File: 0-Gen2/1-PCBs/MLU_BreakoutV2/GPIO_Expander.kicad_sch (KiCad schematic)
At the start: 8 parts, among them U7 MCP23008-E_P

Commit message: [final pass] MLU breakout
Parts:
- JP10, JP8, JP9: footprint Jumper:SolderJumper-3_P1.3mm_Bridged2Bar12_RoundedPad1.0x1.5mm -> Connector_PinHeader_1.27mm:PinHeader_1x03_P1.27mm_Vertical
- U7: footprint Imported Footprints:MCP3008 -> ImportedV2:MCP3008
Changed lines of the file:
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@@
 			)
 		)
-		(property "Footprint" "Jumper:SolderJumper-3_P1.3mm_Bridged2Bar12_RoundedPad1.0x1.5mm"
+		(property "Footprint" "Connector_PinHeader_1.27mm:PinHeader_1x03_P1.27mm_Vertical"
 			(at 93.98 75.946 0)
 			(effects
@@
 			)
 		)
-		(property "Footprint" "Imported Footprints:MCP3008"
+		(property "Footprint" "ImportedV2:MCP3008"
 			(at 163.322 92.71 0)
 			(effects
@@
 			)
 		)
-		(property "Footprint" "Jumper:SolderJumper-3_P1.3mm_Bridged2Bar12_RoundedPad1.0x1.5mm"
+		(property "Footprint" "Connector_PinHeader_1.27mm:PinHeader_1x03_P1.27mm_Vertical"
 			(at 75.438 83.82 0)
 			(effects
@@
 			)
 		)
-		(property "Footprint" "Jumper:SolderJumper-3_P1.3mm_Bridged2Bar12_RoundedPad1.0x1.5mm"
+		(property "Footprint" "Connector_PinHeader_1.27mm:PinHeader_1x03_P1.27mm_Vertical"
 			(at 111.76 111.252 0)
 			(effects

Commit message: before restructure
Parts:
- renumbered C3 to C1, C4 to C2, C5 to C3, JP8 to JP11, JP9 to JP12, JP10 to JP13, U7 to U2
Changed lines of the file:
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@@
 		(dnp no)
 		(fields_autoplaced yes)
-		(property "Reference" "JP8"
+		(property "Reference" "JP11"
 			(at 93.98 72.644 0)
 			(effects
@@
 			(project "MLU_BreakoutV2"
 				(path "/55121ba7-5d22-4fe3-93aa-7f76d75b410c/ff819628-ab19-4c4a-a87c-3aa1c78e0ae1"
-					(reference "JP8")
+					(reference "JP11")
 					(unit 1)
 				)
@@
 		(on_board yes)
 		(dnp no)
-		(property "Reference" "C4"
+		(property "Reference" "C2"
 			(at 120.142 115.8239 0)
 			(effects
@@
 			(project "MLU_BreakoutV2"
 				(path "/55121ba7-5d22-4fe3-93aa-7f76d75b410c/ff819628-ab19-4c4a-a87c-3aa1c78e0ae1"
-					(reference "C4")
+					(reference "C2")
 					(unit 1)
 				)
@@
 		(on_board yes)
 		(dnp no)
-		(property "Reference" "#PWR0141"
+		(property "Reference" "#PWR090"
 			(at 205.232 88.9 0)
 			(effects
@@
 			(project "MLU_BreakoutV2"
 				(path "/55121ba7-5d22-4fe3-93aa-7f76d75b410c/ff819628-ab19-4c4a-a87c-3aa1c78e0ae1"
-					(reference "#PWR0141")
+					(reference "#PWR090")
 					(unit 1)
 				)
@@
 		(dnp no)
 		(fields_autoplaced yes)
-		(property "Reference" "#PWR0146"
+		(property "Reference" "#PWR095"
 			(at 111.76 123.952 0)
 			(effects
@@
 			(project "MLU_BreakoutV2"
 				(path "/55121ba7-5d22-4fe3-93aa-7f76d75b410c/ff819628-ab19-4c4a-a87c-3aa1c78e0ae1"
-					(reference "#PWR0146")
+					(reference "#PWR095")
 					(unit 1)
 				)
@@
 		(on_board yes)
 		(dnp no)
-		(property "Reference" "#PWR0137"
+		(property "Reference" "#PWR086"
 			(at 111.76 79.502 0)
 			(effects
@@
 			(project "MLU_BreakoutV2"
 				(path "/55121ba7-5d22-4fe3-93aa-7f76d75b410c/ff819628-ab19-4c4a-a87c-3aa1c78e0ae1"
-					(reference "#PWR0137")
+					(reference "#PWR086")
 					(unit 1)
 				)
@@
 		(dnp no)
 		(fields_autoplaced yes)
-		(property "Reference" "#PWR0143"
+		(property "Reference" "#PWR092"
 			(at 205.232 99.06 0)
 			(effects
@@
 			(project "MLU_BreakoutV2"
 				(path "/55121ba7-5d22-4fe3-93aa-7f76d75b410c/ff819628-ab19-4c4a-a87c-3aa1c78e0ae1"
-					(reference "#PWR0143")
+					(reference "#PWR092")
 					(unit 1)
 				)
@@
 		(dnp no)
 		(fields_autoplaced yes)
-		(property "Reference" "#PWR0144"
+		(property "Reference" "#PWR093"
 			(at 93.218 102.87 0)
 			(effects
@@
 			(project "MLU_BreakoutV2"
 				(path "/55121ba7-5d22-4fe3-93aa-7f76d75b410c/ff819628-ab19-4c4a-a87c-3aa1c78e0ae1"
-					(reference "#PWR0144")
+					(reference "#PWR093")
 					(unit 1)
 				)
@@
 		(dnp no)
 		(fields_autoplaced yes)
-		(property "Reference" "#PWR0145"
+		(property "Reference" "#PWR094"
 			(at 93.218 109.22 0)
 			(effects
@@
 			(project "MLU_BreakoutV2"
 				(path "/55121ba7-5d22-4fe3-93aa-7f76d75b410c/ff819628-ab19-4c4a-a87c-3aa1c78e0ae1"
-					(reference "#PWR0145")
+					(reference "#PWR094")
 					(unit 1)
 				)
@@
 		(on_board yes)
 		(dnp no)
-		(property "Reference" "C5"
+		(property "Reference" "C3"
 			(at 133.604 115.8239 0)
 			(effects
@@
 			(project "MLU_BreakoutV2"
 				(path "/55121ba7-5d22-4fe3-93aa-7f76d75b410c/ff819628-ab19-4c4a-a87c-3aa1c78e0ae1"
-					(reference "C5")
+					(reference "C3")
 					(unit 1)
 				)
@@
 		(on_board yes)
 		(dnp no)
-		(property "Reference" "#PWR0139"
+		(property "Reference" "#PWR088"
 			(at 127.762 79.502 0)
 			(effects
@@
 			(project "MLU_BreakoutV2"
 				(path "/55121ba7-5d22-4fe3-93aa-7f76d75b410c/ff819628-ab19-4c4a-a87c-3aa1c78e0ae1"
-					(reference "#PWR0139")
+					(reference "#PWR088")
 					(unit 1)
 				)
@@
 		(dnp no)
 		(fields_autoplaced yes)
-		(property "Reference" "U7"
+		(property "Reference" "U2"
 			(at 163.322 74.93 0)
 			(effects
@@
 			(project "MLU_BreakoutV2"
 				(path "/55121ba7-5d22-4fe3-93aa-7f76d75b410c/ff819628-ab19-4c4a-a87c-3aa1c78e0ae1"
-					(reference "U7")
+					(reference "U2")
 					(unit 1)
 				)
@@
 		(dnp no)
 		(fields_autoplaced yes)
-		(property "Reference" "#PWR0147"
+		(property "Reference" "#PWR096"
 			(at 140.462 128.524 0)
 			(effects
@@
 			(project "MLU_BreakoutV2"
 				(path "/55121ba7-5d22-4fe3-93aa-7f76d75b410c/ff819628-ab19-4c4a-a87c-3aa1c78e0ae1"
-					(reference "#PWR0147")
+					(reference "#PWR096")
 					(unit 1)
 				)
@@
 		(on_board yes)
 		(dnp no)
-		(property "Reference" "#PWR0140"
+		(property "Reference" "#PWR089"
 			(at 135.636 79.502 0)
 			(effects
@@
 			(project "MLU_BreakoutV2"
 				(path "/55121ba7-5d22-4fe3-93aa-7f76d75b410c/ff819628-ab19-4c4a-a87c-3aa1c78e0ae1"
-					(reference "#PWR0140")
+					(reference "#PWR089")
 					(unit 1)
 				)
@@
 		(dnp no)
 		(fields_autoplaced yes)
-		(property "Reference" "#PWR0142"
+		(property "Reference" "#PWR091"
 			(at 93.472 96.774 0)
 			(effects
@@
 			(project "MLU_BreakoutV2"
 				(path "/55121ba7-5d22-4fe3-93aa-7f76d75b410c/ff819628-ab19-4c4a-a87c-3aa1c78e0ae1"
-					(reference "#PWR0142")
+					(reference "#PWR091")
 					(unit 1)
 				)
@@
 		(on_board yes)
 		(dnp no)
-		(property "Reference" "C3"
+		(property "Reference" "C1"
 			(at 209.296 87.6299 0)
 			(effects
@@
 			(project "MLU_BreakoutV2"
 				(path "/55121ba7-5d22-4fe3-93aa-7f76d75b410c/ff819628-ab19-4c4a-a87c-3aa1c78e0ae1"
-					(reference "C3")
+					(reference "C1")
 					(unit 1)
 				)
@@
 		(dnp no)
 		(fields_autoplaced yes)
-		(property "Reference" "JP9"
+		(property "Reference" "JP12"
 			(at 75.438 80.264 0)
 			(effects
@@
 			(project "MLU_BreakoutV2"
 				(path "/55121ba7-5d22-4fe3-93aa-7f76d75b410c/ff819628-ab19-4c4a-a87c-3aa1c78e0ae1"
-					(reference "JP9")
+					(reference "JP12")
 					(unit 1)
 				)
@@
 		(on_board yes)
 		(dnp no)
-		(property "Reference" "#PWR0138"
+		(property "Reference" "#PWR087"
 			(at 119.634 79.502 0)
 			(effects
@@
 			(project "MLU_BreakoutV2"
 				(path "/55121ba7-5d22-4fe3-93aa-7f76d75b410c/ff819628-ab19-4c4a-a87c-3aa1c78e0ae1"
-					(reference "#PWR0138")
+					(reference "#PWR087")
 					(unit 1)
 				)
@@
 		(dnp no)
 		(fields_autoplaced yes)
-		(property "Reference" "JP10"
+		(property "Reference" "JP13"
 			(at 109.474 109.9819 90)
 			(effects
@@
 			(project "MLU_BreakoutV2"
 				(path "/55121ba7-5d22-4fe3-93aa-7f76d75b410c/ff819628-ab19-4c4a-a87c-3aa1c78e0ae1"
-					(reference "JP10")
+					(reference "JP13")
 					(unit 1)
 				)

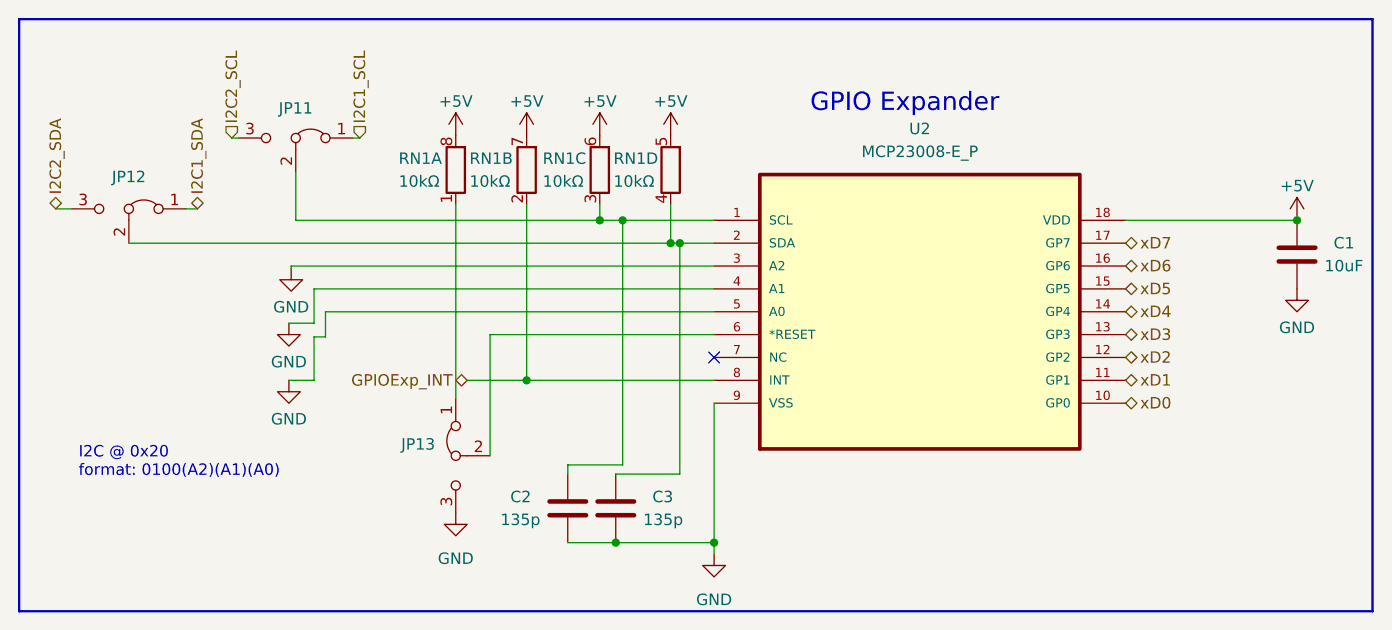
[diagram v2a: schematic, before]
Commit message: [bugfix] rescued footprints
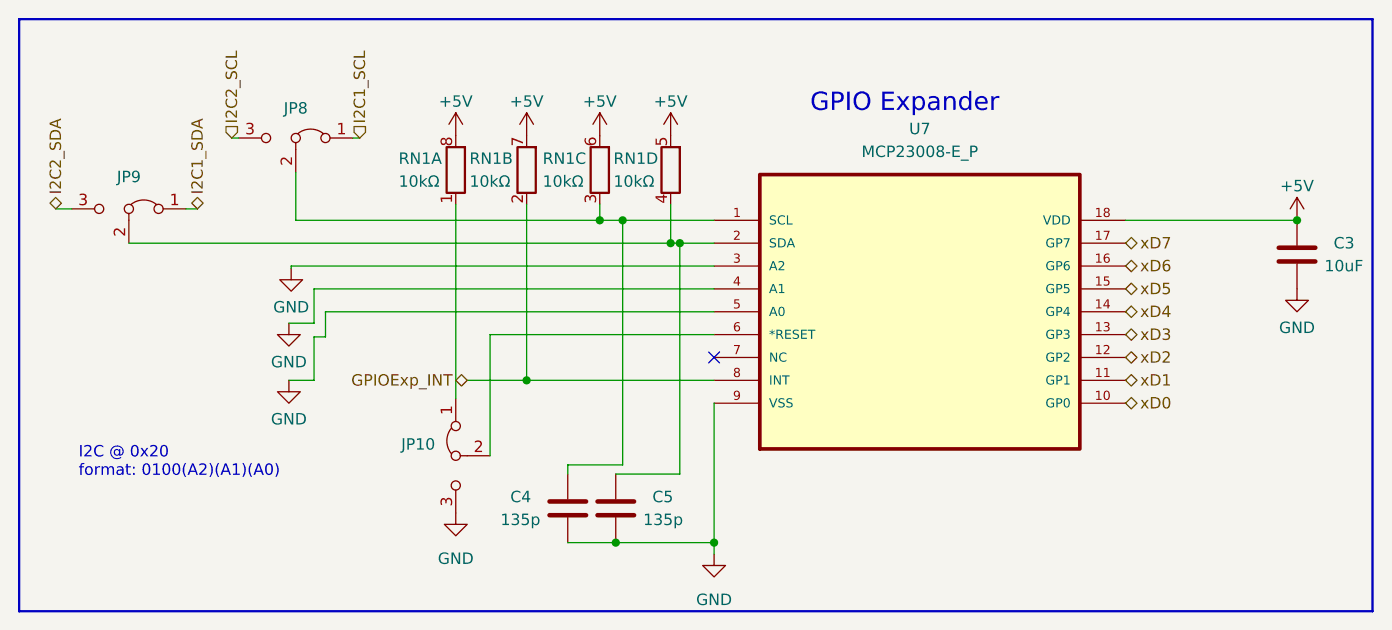
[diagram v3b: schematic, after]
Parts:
- renumbered C1 to C3, C2 to C4, C3 to C5, JP13 to JP10, JP11 to JP8, JP12 to JP9, U2 to U7
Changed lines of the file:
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@@
 		(dnp no)
 		(fields_autoplaced yes)
-		(property "Reference" "JP11"
+		(property "Reference" "JP8"
 			(at 93.98 72.644 0)
 			(effects
@@
 			(project "MLU_BreakoutV2"
 				(path "/55121ba7-5d22-4fe3-93aa-7f76d75b410c/ff819628-ab19-4c4a-a87c-3aa1c78e0ae1"
-					(reference "JP11")
+					(reference "JP8")
 					(unit 1)
 				)
@@
 		(on_board yes)
 		(dnp no)
-		(property "Reference" "C2"
+		(property "Reference" "C4"
 			(at 120.142 115.8239 0)
 			(effects
@@
 			(project "MLU_BreakoutV2"
 				(path "/55121ba7-5d22-4fe3-93aa-7f76d75b410c/ff819628-ab19-4c4a-a87c-3aa1c78e0ae1"
-					(reference "C2")
+					(reference "C4")
 					(unit 1)
 				)
@@
 		(on_board yes)
 		(dnp no)
-		(property "Reference" "#PWR090"
+		(property "Reference" "#PWR0141"
 			(at 205.232 88.9 0)
 			(effects
@@
 			(project "MLU_BreakoutV2"
 				(path "/55121ba7-5d22-4fe3-93aa-7f76d75b410c/ff819628-ab19-4c4a-a87c-3aa1c78e0ae1"
-					(reference "#PWR090")
+					(reference "#PWR0141")
 					(unit 1)
 				)
@@
 		(dnp no)
 		(fields_autoplaced yes)
-		(property "Reference" "#PWR095"
+		(property "Reference" "#PWR0146"
 			(at 111.76 123.952 0)
 			(effects
@@
 			(project "MLU_BreakoutV2"
 				(path "/55121ba7-5d22-4fe3-93aa-7f76d75b410c/ff819628-ab19-4c4a-a87c-3aa1c78e0ae1"
-					(reference "#PWR095")
+					(reference "#PWR0146")
 					(unit 1)
 				)
@@
 		(on_board yes)
 		(dnp no)
-		(property "Reference" "#PWR086"
+		(property "Reference" "#PWR0137"
 			(at 111.76 79.502 0)
 			(effects
@@
 			(project "MLU_BreakoutV2"
 				(path "/55121ba7-5d22-4fe3-93aa-7f76d75b410c/ff819628-ab19-4c4a-a87c-3aa1c78e0ae1"
-					(reference "#PWR086")
+					(reference "#PWR0137")
 					(unit 1)
 				)
@@
 		(dnp no)
 		(fields_autoplaced yes)
-		(property "Reference" "#PWR092"
+		(property "Reference" "#PWR0143"
 			(at 205.232 99.06 0)
 			(effects
@@
 			(project "MLU_BreakoutV2"
 				(path "/55121ba7-5d22-4fe3-93aa-7f76d75b410c/ff819628-ab19-4c4a-a87c-3aa1c78e0ae1"
-					(reference "#PWR092")
+					(reference "#PWR0143")
 					(unit 1)
 				)
@@
 		(dnp no)
 		(fields_autoplaced yes)
-		(property "Reference" "#PWR093"
+		(property "Reference" "#PWR0144"
 			(at 93.218 102.87 0)
 			(effects
@@
 			(project "MLU_BreakoutV2"
 				(path "/55121ba7-5d22-4fe3-93aa-7f76d75b410c/ff819628-ab19-4c4a-a87c-3aa1c78e0ae1"
-					(reference "#PWR093")
+					(reference "#PWR0144")
 					(unit 1)
 				)
@@
 		(dnp no)
 		(fields_autoplaced yes)
-		(property "Reference" "#PWR094"
+		(property "Reference" "#PWR0145"
 			(at 93.218 109.22 0)
 			(effects
@@
 			(project "MLU_BreakoutV2"
 				(path "/55121ba7-5d22-4fe3-93aa-7f76d75b410c/ff819628-ab19-4c4a-a87c-3aa1c78e0ae1"
-					(reference "#PWR094")
+					(reference "#PWR0145")
 					(unit 1)
 				)
@@
 		(on_board yes)
 		(dnp no)
-		(property "Reference" "C3"
+		(property "Reference" "C5"
 			(at 133.604 115.8239 0)
 			(effects
@@
 			(project "MLU_BreakoutV2"
 				(path "/55121ba7-5d22-4fe3-93aa-7f76d75b410c/ff819628-ab19-4c4a-a87c-3aa1c78e0ae1"
-					(reference "C3")
+					(reference "C5")
 					(unit 1)
 				)
@@
 		(on_board yes)
 		(dnp no)
-		(property "Reference" "#PWR088"
+		(property "Reference" "#PWR0139"
 			(at 127.762 79.502 0)
 			(effects
@@
 			(project "MLU_BreakoutV2"
 				(path "/55121ba7-5d22-4fe3-93aa-7f76d75b410c/ff819628-ab19-4c4a-a87c-3aa1c78e0ae1"
-					(reference "#PWR088")
+					(reference "#PWR0139")
 					(unit 1)
 				)
@@
 		(dnp no)
 		(fields_autoplaced yes)
-		(property "Reference" "U2"
+		(property "Reference" "U7"
 			(at 163.322 74.93 0)
 			(effects
@@
 			(project "MLU_BreakoutV2"
 				(path "/55121ba7-5d22-4fe3-93aa-7f76d75b410c/ff819628-ab19-4c4a-a87c-3aa1c78e0ae1"
-					(reference "U2")
+					(reference "U7")
 					(unit 1)
 				)
@@
 		(dnp no)
 		(fields_autoplaced yes)
-		(property "Reference" "#PWR096"
+		(property "Reference" "#PWR0147"
 			(at 140.462 128.524 0)
 			(effects
@@
 			(project "MLU_BreakoutV2"
 				(path "/55121ba7-5d22-4fe3-93aa-7f76d75b410c/ff819628-ab19-4c4a-a87c-3aa1c78e0ae1"
-					(reference "#PWR096")
+					(reference "#PWR0147")
 					(unit 1)
 				)
@@
 		(on_board yes)
 		(dnp no)
-		(property "Reference" "#PWR089"
+		(property "Reference" "#PWR0140"
 			(at 135.636 79.502 0)
 			(effects
@@
 			(project "MLU_BreakoutV2"
 				(path "/55121ba7-5d22-4fe3-93aa-7f76d75b410c/ff819628-ab19-4c4a-a87c-3aa1c78e0ae1"
-					(reference "#PWR089")
+					(reference "#PWR0140")
 					(unit 1)
 				)
@@
 		(dnp no)
 		(fields_autoplaced yes)
-		(property "Reference" "#PWR091"
+		(property "Reference" "#PWR0142"
 			(at 93.472 96.774 0)
 			(effects
@@
 			(project "MLU_BreakoutV2"
 				(path "/55121ba7-5d22-4fe3-93aa-7f76d75b410c/ff819628-ab19-4c4a-a87c-3aa1c78e0ae1"
-					(reference "#PWR091")
+					(reference "#PWR0142")
 					(unit 1)
 				)
@@
 		(on_board yes)
 		(dnp no)
-		(property "Reference" "C1"
+		(property "Reference" "C3"
 			(at 209.296 87.6299 0)
 			(effects
@@
 			(project "MLU_BreakoutV2"
 				(path "/55121ba7-5d22-4fe3-93aa-7f76d75b410c/ff819628-ab19-4c4a-a87c-3aa1c78e0ae1"
-					(reference "C1")
+					(reference "C3")
 					(unit 1)
 				)
@@
 		(dnp no)
 		(fields_autoplaced yes)
-		(property "Reference" "JP12"
+		(property "Reference" "JP9"
 			(at 75.438 80.264 0)
 			(effects
@@
 			(project "MLU_BreakoutV2"
 				(path "/55121ba7-5d22-4fe3-93aa-7f76d75b410c/ff819628-ab19-4c4a-a87c-3aa1c78e0ae1"
-					(reference "JP12")
+					(reference "JP9")
 					(unit 1)
 				)
@@
 		(on_board yes)
 		(dnp no)
-		(property "Reference" "#PWR087"
+		(property "Reference" "#PWR0138"
 			(at 119.634 79.502 0)
 			(effects
@@
 			(project "MLU_BreakoutV2"
 				(path "/55121ba7-5d22-4fe3-93aa-7f76d75b410c/ff819628-ab19-4c4a-a87c-3aa1c78e0ae1"
-					(reference "#PWR087")
+					(reference "#PWR0138")
 					(unit 1)
 				)
@@
 		(dnp no)
 		(fields_autoplaced yes)
-		(property "Reference" "JP13"
+		(property "Reference" "JP10"
 			(at 109.474 109.9819 90)
 			(effects
@@
 			(project "MLU_BreakoutV2"
 				(path "/55121ba7-5d22-4fe3-93aa-7f76d75b410c/ff819628-ab19-4c4a-a87c-3aa1c78e0ae1"
-					(reference "JP13")
+					(reference "JP10")
 					(unit 1)
 				)
